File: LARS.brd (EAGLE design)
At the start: 101.6 x 54.3 mm, 19 parts, among them U1 ARDUINO-MEGAFULL

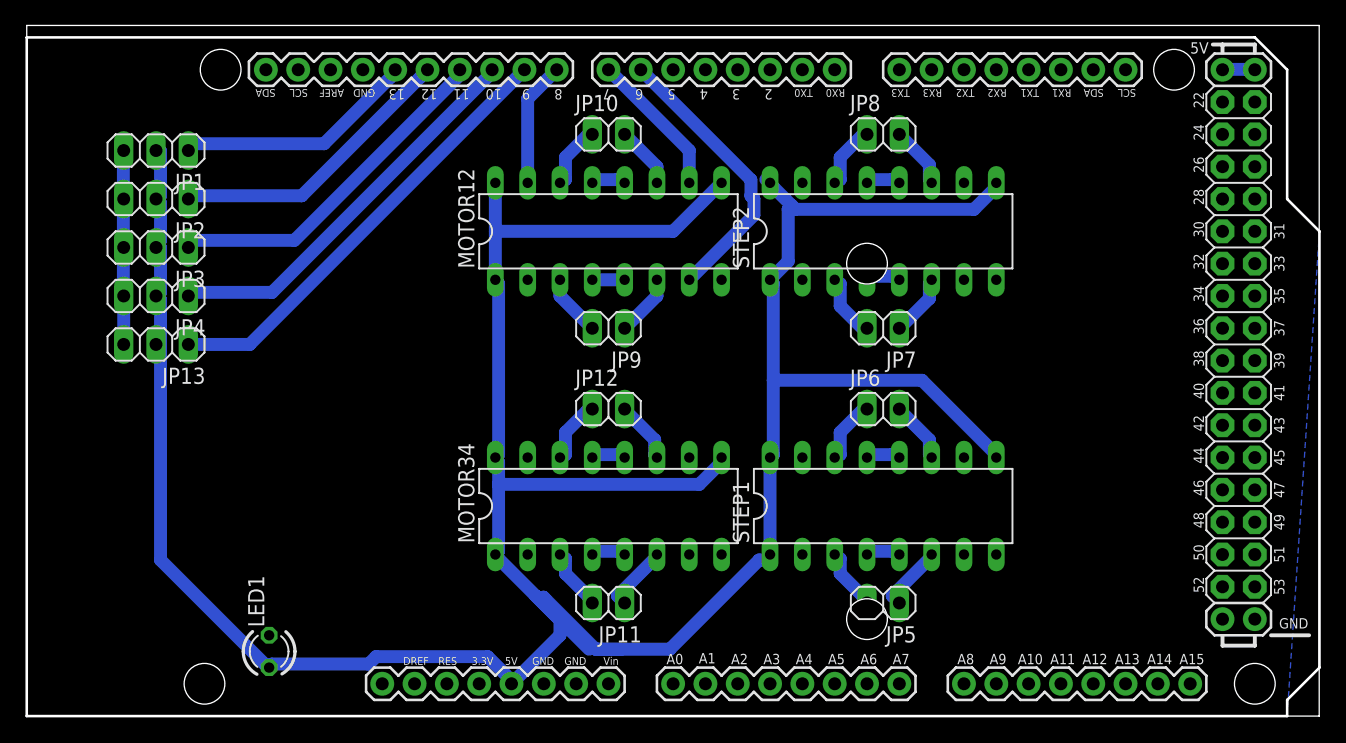
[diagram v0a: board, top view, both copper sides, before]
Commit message: parei de mexer na placa pra tentar fazer o robô móvel
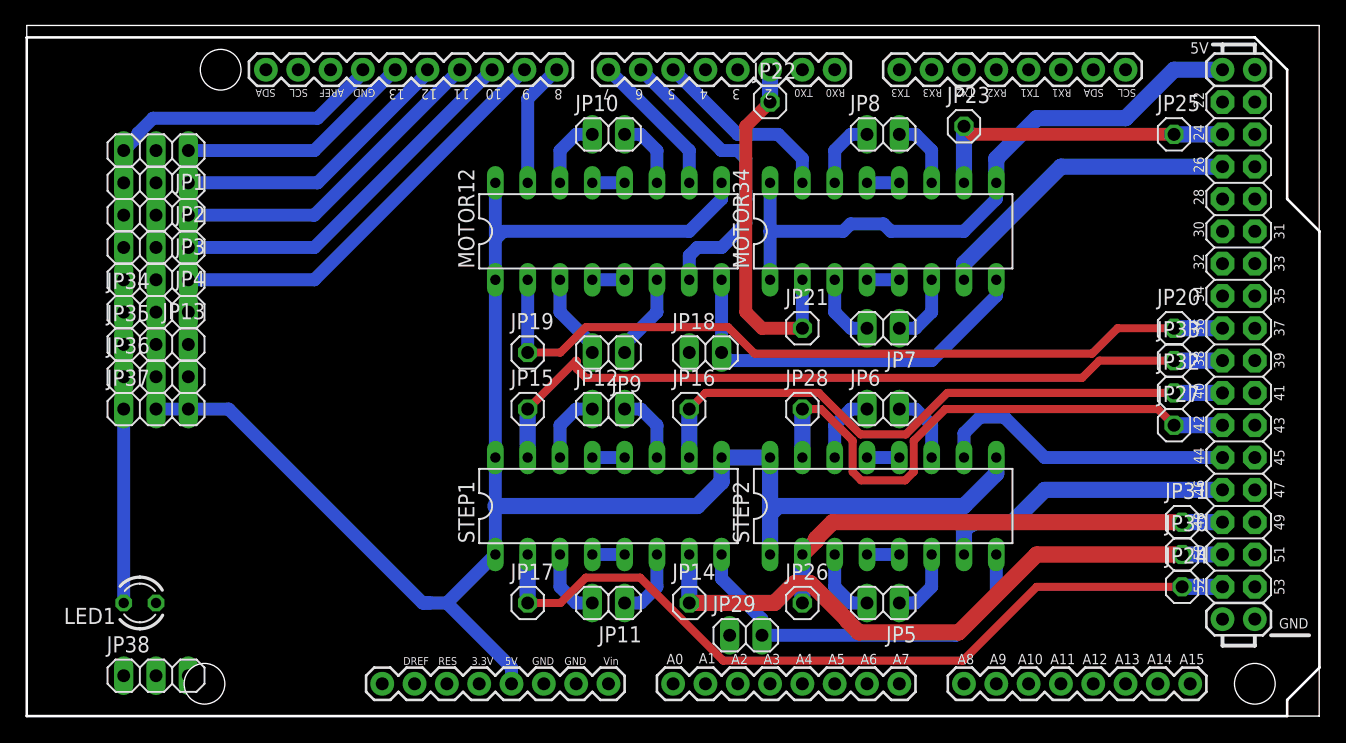
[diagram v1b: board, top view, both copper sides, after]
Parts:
- added JP14, JP15, JP16, JP17, JP19, JP20, JP21, JP22, JP23, JP24, JP25, JP26, JP27, JP28, JP30, JP31, JP32, JP33: (no value), pinhead:1X01
- added JP18, JP29: (no value), pinhead:1X02
- added JP34, JP35, JP36, JP37, JP38: (no value), pinhead:1X03
- moved MOTOR34 30.5 mm to (67.3, 38.1)
- moved STEP1 21.6 mm to (45.7, 16.5)
- moved STEP2 21.6 mm to (67.3, 16.5)
- moved LED1 10.9 mm to (8.89, 8.89), turned to 180 degrees
- moved JP13 5.08 mm to (10.2, 34.3)
- moved JP4 3.81 mm to (10.2, 36.8)
- moved JP3 2.54 mm to (10.2, 39.4)
- moved JP9 1.91 mm to (45.7, 28.6)
- moved JP2 1.27 mm to (10.2, 41.9)
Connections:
- removed net INC2: STEP2.10
- removed net N$3: U1.5
- new net OUTB2: MOTOR34.7, U1.26
- new net OUTD2: MOTOR34.15, U1.5
- new net PIN2: JP21.1, JP22.1, MOTOR34.2, U1.2
- new net PIN24: JP23.1, JP25.1, MOTOR34.10, U1.24
- new net PIN38: JP19.1, JP20.1, MOTOR12.2, U1.36
- new net STPA1: JP17.1, JP24.1, STEP1.2, U1.52
- new net STPA2: JP26.1, JP31.1, STEP2.2, U1.48
- new net STPB1: JP14.1, JP30.1, STEP1.7, U1.50
- new net STPB2: STEP2.7, U1.46
- new net STPC1: JP16.1, JP32.1, STEP1.10, U1.40
- new net STPC2: STEP2.10, U1.44
- new net STPD1: JP15.1, JP33.1, STEP1.15, U1.38
- new net STPD2: JP27.1, JP28.1, STEP2.15, U1.42
- new net VCC3: JP29.2, STEP1.8, STEP2.8
- net GND: now also JP18.1, JP29.1, JP34.3, JP35.3, JP36.3, JP37.3, JP38.3
- net SERVO1: now also JP35.1
- net SERVO2: now also JP34.1
- net SERVO3: now also JP36.1
- net SERVO4: now also JP37.1
- net SERVO5: now also JP38.1
- net STP1: now also STEP2.3; no longer STEP1.3
- net STP13: now also STEP1.3; no longer MOTOR34.3
- net STP14: now also STEP1.6; no longer MOTOR34.6
- net STP15: now also STEP1.11; no longer MOTOR34.11
- net STP16: now also STEP1.14; no longer MOTOR34.14
- net STP2: now also STEP2.6; no longer STEP1.6
- net STP3: now also STEP2.11; no longer STEP1.11
- net STP4: now also STEP2.14; no longer STEP1.14
- net STP5: now also MOTOR34.3; no longer STEP2.3
- net STP6: now also MOTOR34.6; no longer STEP2.6
- net STP7: now also MOTOR34.11; no longer STEP2.11
- net STP8: now also MOTOR34.14; no longer STEP2.14
- net VCC: now also JP34.2, JP35.2, JP36.2, JP37.2, JP38.2
- net VCC2: now also JP18.2; no longer STEP1.8, STEP2.8
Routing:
- net STPA1: track 0.00 -> 64.4 mm
- net PIN38: track 0.00 -> 62.8 mm
- net STPD1: track 0.00 -> 61.5 mm
- net STPB1: track 0.00 -> 50.5 mm
- net STPC1: track 0.00 -> 48.9 mm
- net STPD2: track 0.00 -> 44.9 mm
- net GND: track 36.7 -> 77.6 mm
- net STPA2: track 0.00 -> 38.0 mm
- net VCC: track 252.6 -> 216.6 mm
- net VCC2: track 0.00 -> 30.9 mm
- net VCC3: track 0.00 -> 30.6 mm
- net PIN2: track 0.00 -> 28.6 mm
- net PIN24: track 0.00 -> 25.0 mm
- net OUTB2: track 0.00 -> 24.7 mm
- net STPC2: track 0.00 -> 24.1 mm
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- removed copper zone on layer 16, net GND
